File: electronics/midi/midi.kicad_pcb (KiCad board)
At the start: 2 copper layers, 20.3 x 38.1 mm, 13 parts, among them P1 DIN-5, P2 CONN_01X04, P3 UART

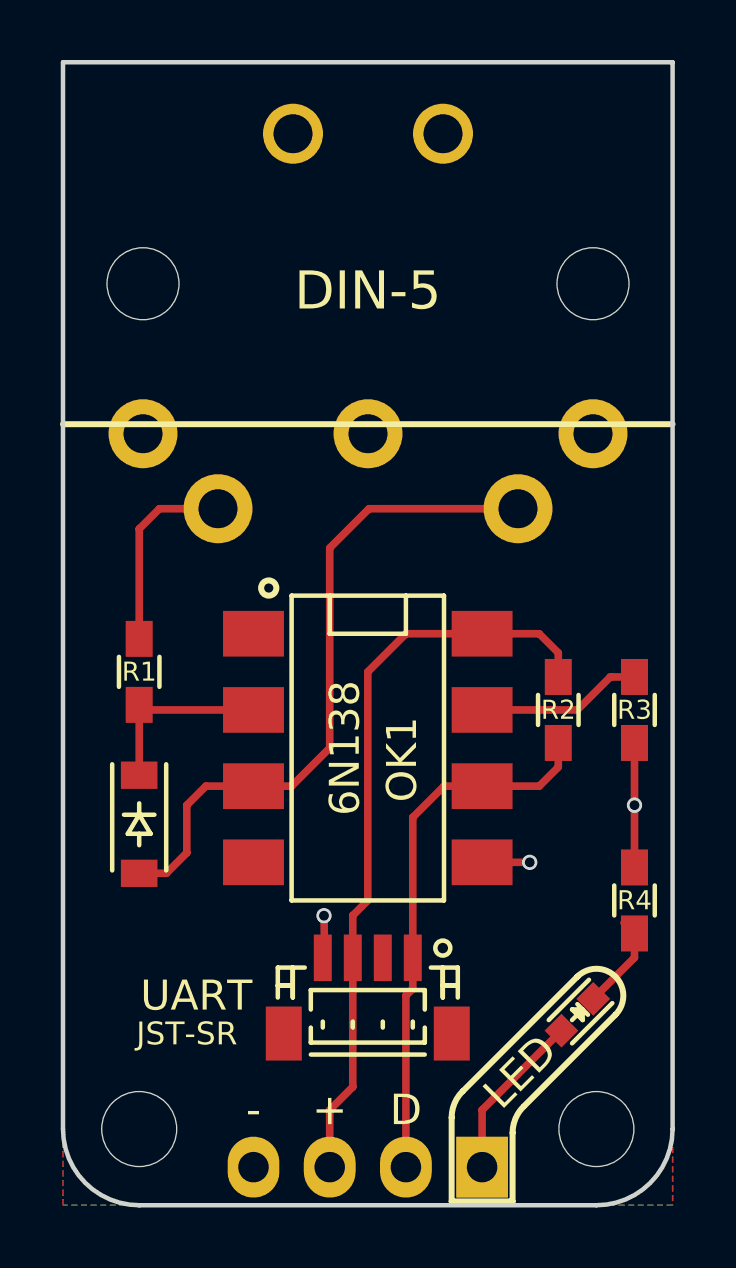
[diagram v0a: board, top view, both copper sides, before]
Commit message: Start updating MIDI_IN board
- add decoupling cap
- change LED polarity
- change 4-pin header to 3-pin
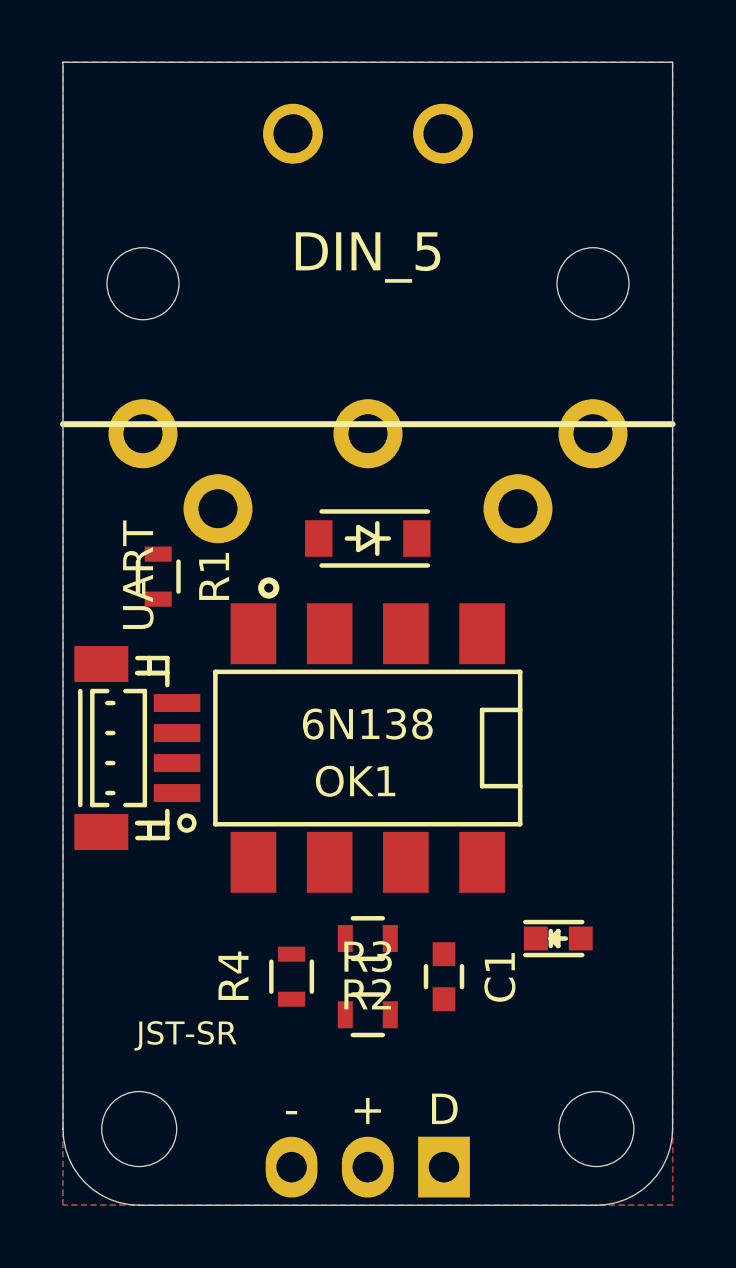
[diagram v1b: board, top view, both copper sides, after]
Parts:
- added C1: 0.1u, Capacitors_SMD:C_0603, F.Cu at (154.9, 111.8)
- P1: value DIN-5 -> DIN_5; footprint SDS-50J -> Connect:SDS-50J
- P2: value CONN_01X04 -> HEADER; footprint Pin_Headers:Pin_Header_Straight_1x04 -> Pin_Headers:Pin_Header_Straight_1x03
- R1, R2: footprint Resistors_SMD:R_0603_HandSoldering -> Resistors_SMD:R_0603
- R3: value 1k -> 220; footprint Resistors_SMD:R_0603_HandSoldering -> Resistors_SMD:R_0603
- R4: value 220 -> 1k; footprint Resistors_SMD:R_0603_HandSoldering -> Resistors_SMD:R_0603
- moved R3 13.5 mm to (152.4, 113.0), turned to 0 degrees
- moved D1 12.2 mm to (152.4, 97.2), turned to 180 degrees
- moved R4 11.7 mm to (149.9, 111.8), turned to 90 degrees
- moved P3 11.2 mm to (144.8, 104.1), turned to 90 degrees
- moved R2 9.92 mm to (152.4, 110.5), turned to 180 degrees
- moved R1 3.24 mm to (145.4, 98.4), turned to 270 degrees
- moved D2 2.62 mm to (158.8, 110.5), turned to 0 degrees
- moved P2 1.27 mm to (154.9, 118.1)
- turned OK1 to 180 degrees
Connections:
- D2 pad 2: /LED -> Net-(D2-Pad2)
- OK1 pad 6: /MIDI -> Net-(D2-Pad1)
- P2 pad 1: /LED -> Net-(D2-Pad1)
- P2 pad 2: /MIDI -> +3V3
- P2 pad 3: +3V3 -> GND
- P3 pad 1: /MIDI -> Net-(D2-Pad1)
- R1 pad 1: Net-(D1-Pad1) -> Net-(P1-Pad4)
- R1 pad 2: Net-(P1-Pad4) -> Net-(D1-Pad1)
- R2 pad 1: +3V3 -> Net-(D2-Pad1)
- R2 pad 2: /MIDI -> +3V3
- R3 pad 1: GND -> Net-(D2-Pad2)
- R3 pad 2: Net-(OK1-Pad7) -> +3V3
- R4 pad 2: Net-(D2-Pad1) -> Net-(OK1-Pad7)
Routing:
- net +3V3: track 25.2 -> 0.52 mm
- net Net-(D1-Pad2): track 22.5 -> 0.00 mm
- net /MIDI: track 18.1 -> 0.00 mm
- net GND: track 7.38 -> 0.24 mm, vias 3 -> 0
- net Net-(P1-Pad4): track 6.57 -> 0.00 mm
- net Net-(D1-Pad1): track 6.47 -> 0.24 mm
- net Net-(OK1-Pad7): track 5.54 -> 0.00 mm
- net /LED: track 5.01 -> 0.00 mm
- net Net-(D2-Pad1): track 3.25 -> 0.00 mm
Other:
- board text removed: "LED"
